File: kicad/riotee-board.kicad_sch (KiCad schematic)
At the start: 0 parts

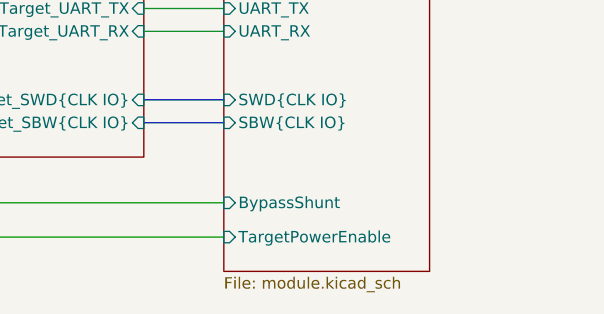
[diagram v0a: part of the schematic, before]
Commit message: copy in module schematics
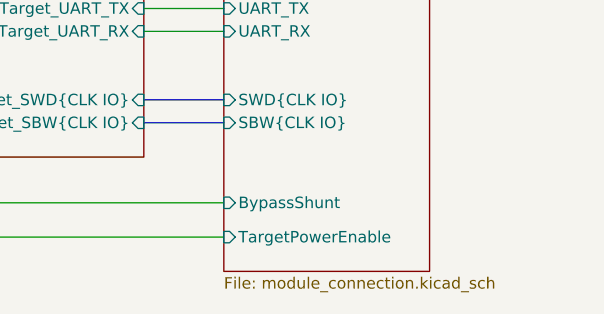
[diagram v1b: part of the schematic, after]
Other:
- sheet Riotee Module: file module.kicad_sch -> module_connection.kicad_sch
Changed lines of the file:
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@@
 (kicad_sch
-	(version 20231120)
+	(version 20250114)
 	(generator "eeschema")
-	(generator_version "8.0")
+	(generator_version "9.0")
 	(paper "A4")
 	(wire
@@
 		(at 62.23 90.17)
 		(size 52.07 50.8)
+		(exclude_from_sim no)
+		(in_bom yes)
+		(on_board yes)
+		(dnp no)
 		(fields_autoplaced yes)
 		(stroke
@@
 		(at 203.2 100.33)
 		(size 22.86 40.64)
+		(exclude_from_sim no)
+		(in_bom yes)
+		(on_board yes)
+		(dnp no)
 		(fields_autoplaced yes)
 		(stroke
@@
 			)
 		)
-		(property "Sheetfile" "module.kicad_sch"
+		(property "Sheetfile" "module_connection.kicad_sch"
 			(at 203.2 141.5546 0)
 			(effects
@@
 		(at 139.7 100.33)
 		(size 54.61 27.94)
+		(exclude_from_sim no)
+		(in_bom yes)
+		(on_board yes)
+		(dnp no)
 		(fields_autoplaced yes)
 		(stroke
@@
 		(at 62.23 67.31)
 		(size 52.07 10.16)
+		(exclude_from_sim no)
+		(in_bom yes)
+		(on_board yes)
+		(dnp no)
 		(fields_autoplaced yes)
 		(stroke
@@
 		)
 	)
+	(embedded_fonts no)
 )

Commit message: unify module and board
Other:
- sheet Riotee Module renamed Module Connection
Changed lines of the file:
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@@
 			(color 0 0 0 0.0000)
 		)
-		(property "Sheetname" "Riotee Module"
+		(property "Sheetname" "Module Connection"
 			(at 203.2 99.6184 0)
 			(effects
